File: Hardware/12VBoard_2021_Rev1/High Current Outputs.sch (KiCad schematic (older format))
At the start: 4 parts

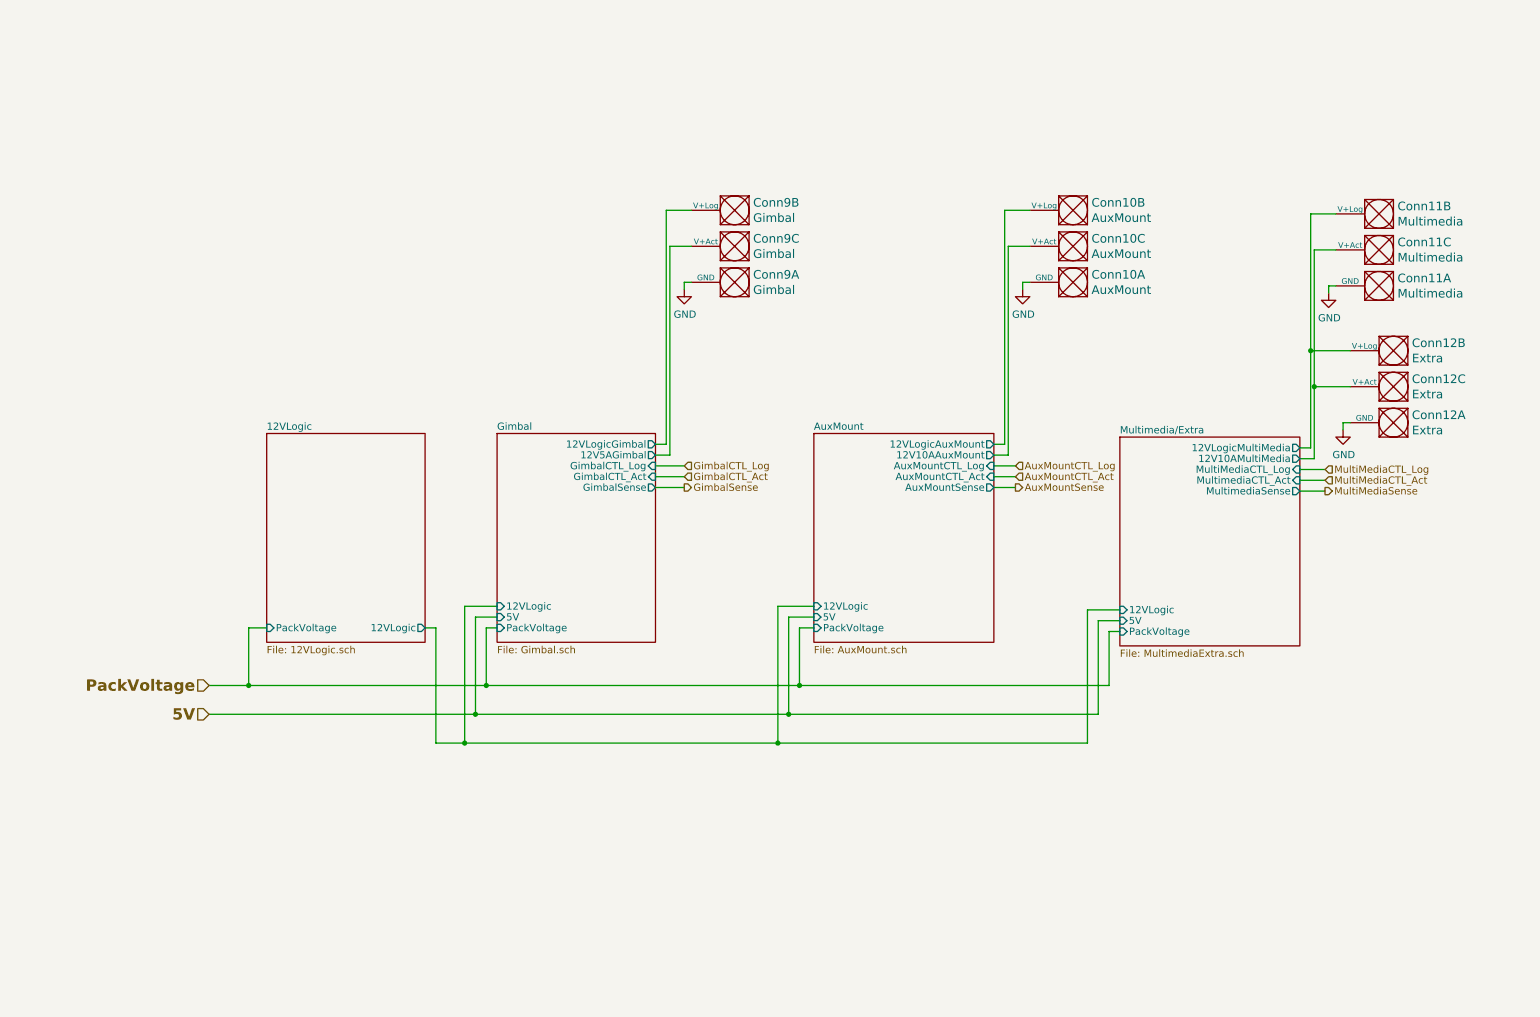
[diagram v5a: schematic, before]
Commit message: changed to big bucks
changed to the bucks used in Master due to a realization in the inductor sizing for the LM5116. It would be much bigger than previous years.
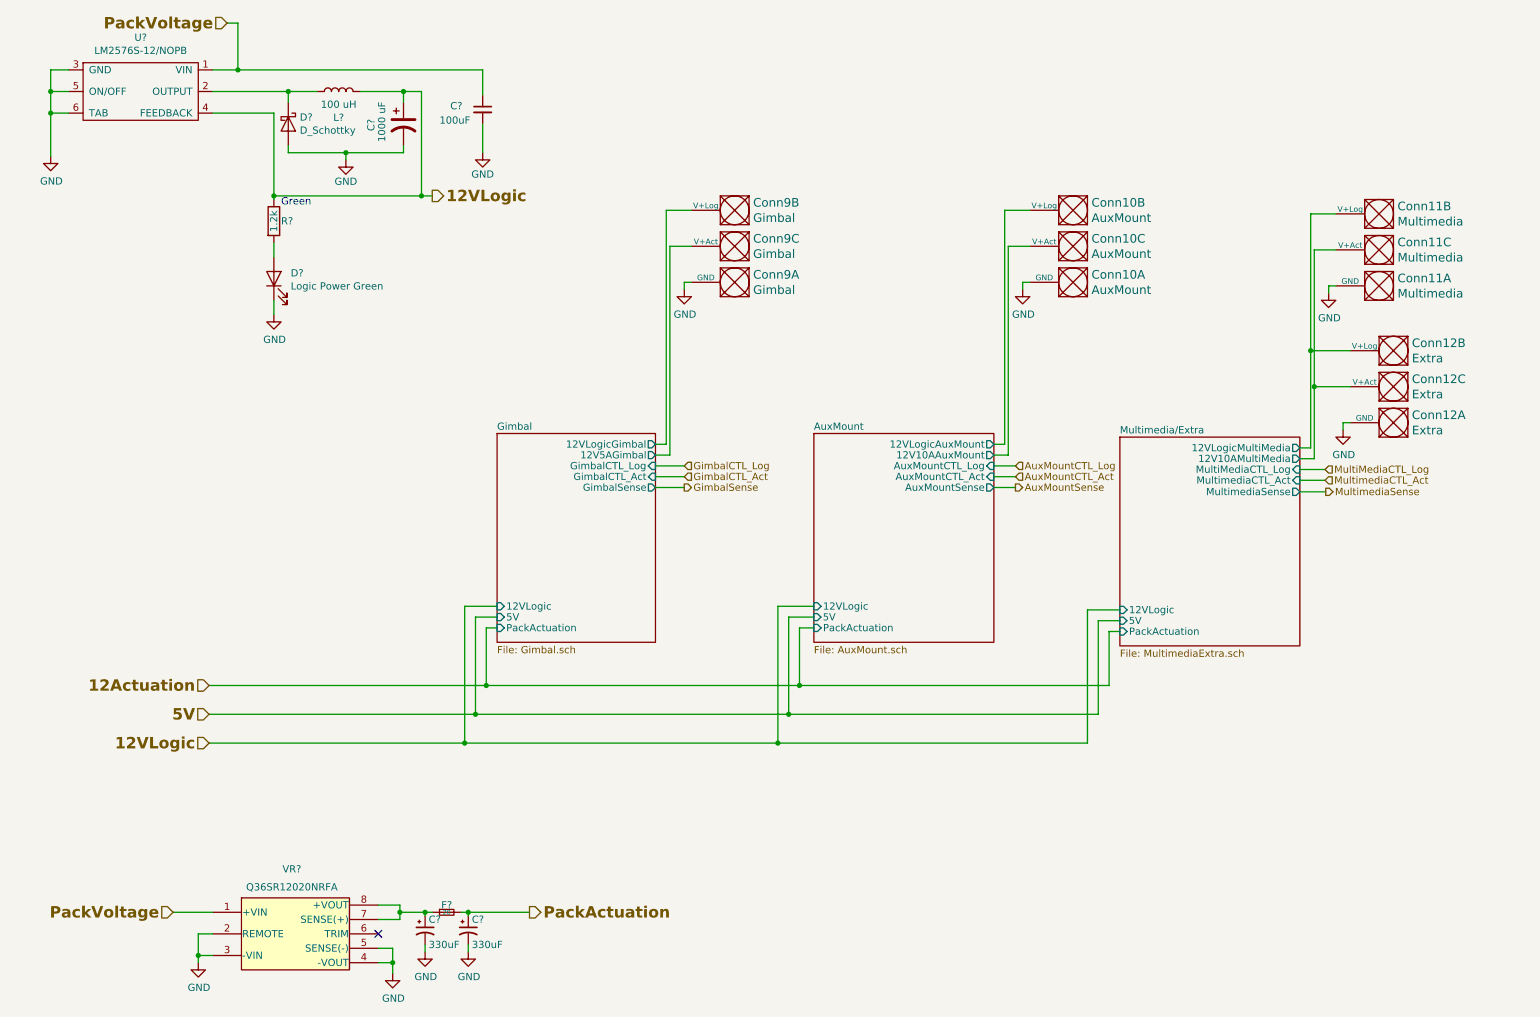
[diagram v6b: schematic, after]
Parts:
- added C? (x2): 330uF, symbol Device:CP1_Small
- added C?: 100uF, Capacitor_SMD:C_0603_1608Metric_Pad1.05x0.95mm_HandSolder, symbol Device:C_Small
- added C?: 1000 uF, Capacitor_THT:CP_Radial_D10.0mm_P5.00mm, symbol Device:CP1
- added D?: D_Schottky, Diode_THT:D_DO-201AD_P5.08mm_Vertical_KathodeUp, symbol Device:D_Schottky
- added D?: Logic Power Green, Diode_SMD:D_0603_1608Metric_Pad1.05x0.95mm_HandSolder, symbol Device:LED
- added F?: 20, symbol Device:Fuse_Small
- added L?: 100 uH, Inductor_SMD:L_0603_1608Metric_Pad1.05x0.95mm_HandSolder, symbol Device:L
- added R?: 1.2k, Resistor_SMD:R_0603_1608Metric_Pad1.05x0.95mm_HandSolder, symbol Device:R
- added U?: LM2576S-12/NOPB, MRDT_Devices:LM2576, symbol 12VBoard_2021_Rev1-rescue:LM2576D2TR4-MRDT_Devices
- added VR?: Q36SR12020NRFA, symbol MRDT_Devices:Q36SR12020NRFA
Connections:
- net GND: now also C?.2, C?.2, C?.2, C?.2, D?.1 (K), D?.2 (A), U?.3 (GND), U?.5 (ON/OFF), U?.6 (TAB), VR?.2 (REMOTE), VR?.3 (-VIN), VR?.4 (-VOUT), VR?.5 (SENSE(-))
- net PackVoltage: now also C?.1, U?.1 (VIN), VR?.1 (+VIN)
- new net: C?.1, F?.1, VR?.7 (SENSE(+)), VR?.8 (+VOUT)
- new net: D?.1 (K), L?.1, U?.2 (OUTPUT)
- new net: D?.2 (A), R?.2
- new net 12VLogic: C?.1, L?.2, R?.1, U?.4 (FEEDBACK)
- new net PackActuation: C?.1, F?.2
- no-connect marks 0 -> 1
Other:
- note added: "Green"

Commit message: Started work on updated layout
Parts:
- C10, C11: renamed from C?; footprint (none) -> Capacitor_THT:CP_Radial_D8.0mm_P3.50mm
- F2: renamed from F?; footprint (none) -> MRDT_Passives:ATC_Fuse_Block
- VR1: renamed from VR?; footprint (none) -> MRDT_Actives:Q36SR12020NRFA
- gave numbers to parts that had none: 7
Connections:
- net PackActuation renamed 12VActuation
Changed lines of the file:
@@
 F5 "5V" I L 6025 4800 49
 F6 "12VLogicAuxMount" O R 7275 3600 50
-F7 "PackActuation" I L 6025 4875 50
+F7 "12VActuation" I L 6025 4875 50
 F8 "12VLogic" I L 6025 4725 50
 F9 "AuxMountCTL_Log" I R 7275 3750 50
@@
 F5 "12VLogicGimbal" O R 4925 3600 50
 F6 "5V" I L 3825 4800 50
-F7 "PackActuation" I L 3825 4875 50
+F7 "12VActuation" I L 3825 4875 50
 F8 "12VLogic" I L 3825 4725 50
 F9 "GimbalCTL_Log" I R 4925 3750 50
@@
 F5 "5V" I L 8150 4825 49
 F6 "12VLogicMultiMedia" O R 9400 3625 50
-F7 "PackActuation" I L 8150 4900 50
+F7 "12VActuation" I L 8150 4900 50
 F8 "12VLogic" I L 8150 4750 50
 F9 "MultiMediaCTL_Log" I R 9400 3775 50
@@
 MultiMediaCTL_Log
 $Comp
-L MRDT_Devices:Q36SR12020NRFA VR?
+L MRDT_Devices:Q36SR12020NRFA VR1
 U 1 1 60547610
 P 2050 7250
-F 0 "VR?" H 2400 7950 50  0000 C CNN
+F 0 "VR1" H 2400 7950 50  0000 C CNN
 F 1 "Q36SR12020NRFA" H 2400 7825 50  0000 C CNN
-F 2 "" H 2350 8050 50  0001 C CNN
+F 2 "MRDT_Actives:Q36SR12020NRFA" H 2350 8050 50  0001 C CNN
 F 3 "" H 2350 8050 50  0001 C CNN
 	1    2050 7250
@@
 	1850 6850 1575 6850
 $Comp
-L power:GND #PWR?
+L power:GND #PWR0101
 U 1 1 6054F874
 P 1750 7200
-F 0 "#PWR?" H 1750 6950 50  0001 C CNN
+F 0 "#PWR0101" H 1750 6950 50  0001 C CNN
 F 1 "GND" H 1755 7027 50  0000 C CNN
 F 2 "" H 1750 7200 50  0001 C CNN
@@
 Connection ~ 3100 7200
 $Comp
-L power:GND #PWR?
+L power:GND #PWR0102
 U 1 1 60562828
 P 3100 7275
-F 0 "#PWR?" H 3100 7025 50  0001 C CNN
+F 0 "#PWR0102" H 3100 7025 50  0001 C CNN
 F 1 "GND" H 3105 7102 50  0000 C CNN
 F 2 "" H 3100 7275 50  0001 C CNN
@@
 	3150 6850 3150 6900
 $Comp
-L Device:CP1_Small C?
+L Device:CP1_Small C10
 U 1 1 6056D755
 P 3325 6975
-F 0 "C?" H 3350 7050 50  0000 L CNN
+F 0 "C10" H 3350 7050 50  0000 L CNN
 F 1 "330uF" H 3350 6875 50  0000 L CNN
-F 2 "" H 3325 6975 50  0001 C CNN
+F 2 "Capacitor_THT:CP_Radial_D8.0mm_P3.50mm" H 3325 6975 50  0001 C CNN
 F 3 "~" H 3325 6975 50  0001 C CNN
 	1    3325 6975
@@
 	3625 6850 4050 6850
 Text HLabel 4050 6850 2    79   Output ~ 16
-PackActuation
-$Comp
-L power:GND #PWR?
+12VActuation
+$Comp
+L power:GND #PWR0103
 U 1 1 60583D08
 P 3325 7125
-F 0 "#PWR?" H 3325 6875 50  0001 C CNN
+F 0 "#PWR0103" H 3325 6875 50  0001 C CNN
 F 1 "GND" H 3330 6952 50  0000 C CNN
 F 2 "" H 3325 7125 50  0001 C CNN
@@
 	3325 7075 3325 7125
 $Comp
-L Device:CP1_Small C?
+L Device:CP1_Small C11
 U 1 1 605915AE
 P 3625 6975
-F 0 "C?" H 3650 7050 50  0000 L CNN
+F 0 "C11" H 3650 7050 50  0000 L CNN
 F 1 "330uF" H 3650 6875 50  0000 L CNN
-F 2 "" H 3625 6975 50  0001 C CNN
+F 2 "Capacitor_THT:CP_Radial_D8.0mm_P3.50mm" H 3625 6975 50  0001 C CNN
 F 3 "~" H 3625 6975 50  0001 C CNN
 	1    3625 6975
@@
 	3625 6875 3625 6850
 $Comp
-L power:GND #PWR?
+L power:GND #PWR0104
 U 1 1 605915B5
 P 3625 7125
-F 0 "#PWR?" H 3625 6875 50  0001 C CNN
+F 0 "#PWR0104" H 3625 6875 50  0001 C CNN
 F 1 "GND" H 3630 6952 50  0000 C CNN
 F 2 "" H 3625 7125 50  0001 C CNN
@@
 	3625 7075 3625 7125
 $Comp
-L Device:Fuse_Small F?
+L Device:Fuse_Small F2
 U 1 1 60594467
 P 3475 6850
-F 0 "F?" H 3475 6900 50  0000 C CNN
+F 0 "F2" H 3475 6900 50  0000 C CNN
 F 1 "20" H 3475 6850 31  0000 C CNN
-F 2 "" H 3475 6850 50  0001 C CNN
+F 2 "MRDT_Passives:ATC_Fuse_Block" H 3475 6850 50  0001 C CNN
 F 3 "~" H 3475 6850 50  0001 C CNN
 	1    3475 6850
@@
 AR Path="/5F74F36B/5F971CD6/605D6402" Ref="#PWR?"  Part="1"
 AR Path="/5F74F36B/5F8236F9/605D6402" Ref="#PWR?"  Part="1"
-AR Path="/5F74F36B/605D6402" Ref="#PWR?"  Part="1"
+AR Path="/5F74F36B/605D6402" Ref="#PWR0105"  Part="1"
 AR Path="/5F74F36B/5FB68F3E/605D6402" Ref="#PWR?"  Part="1"
-F 0 "#PWR?" H 2275 2450 50  0001 C CNN
+F 0 "#PWR0105" H 2275 2450 50  0001 C CNN
 F 1 "GND" H 2280 2527 50  0000 C CNN
 F 2 "" H 2275 2700 50  0001 C CNN
@@
 AR Path="/5F74F36B/5F971CD6/605D6408" Ref="D?"  Part="1"
 AR Path="/5F74F36B/5F8236F9/605D6408" Ref="D?"  Part="1"
-AR Path="/5F74F36B/605D6408" Ref="D?"  Part="1"
+AR Path="/5F74F36B/605D6408" Ref="D1"  Part="1"
 AR Path="/5F74F36B/5FB68F3E/605D6408" Ref="D?"  Part="1"
-F 0 "D?" V 2314 2333 50  0000 R CNN
+F 0 "D1" V 2314 2333 50  0000 R CNN
 F 1 "Logic Power Green" V 2223 2333 50  0000 R CNN
 F 2 "Diode_SMD:D_0603_1608Metric_Pad1.05x0.95mm_HandSolder" H 2275 2450 50  0001 C CNN
@@
 AR Path="/5F74F36B/5F971CD6/605D63FC" Ref="R?"  Part="1"
 AR Path="/5F74F36B/5F8236F9/605D63FC" Ref="R?"  Part="1"
-AR Path="/5F74F36B/605D63FC" Ref="R?"  Part="1"
+AR Path="/5F74F36B/605D63FC" Ref="R8"  Part="1"
 AR Path="/5F74F36B/5FB68F3E/605D63FC" Ref="R?"  Part="1"
-F 0 "R?" H 2325 2050 50  0000 L CNN
+F 0 "R8" H 2325 2050 50  0000 L CNN
 F 1 "1.2k" V 2275 1975 50  0000 L CNN
 F 2 "Resistor_SMD:R_0603_1608Metric_Pad1.05x0.95mm_HandSolder" V 2205 2050 50  0001 C CNN
@@
 AR Path="/5F74F223/605D63F4" Ref="#PWR?"  Part="1"
 AR Path="/5F74F36B/5F8236F9/605D63F4" Ref="#PWR?"  Part="1"
-AR Path="/5F74F36B/605D63F4" Ref="#PWR?"  Part="1"
+AR Path="/5F74F36B/605D63F4" Ref="#PWR0106"  Part="1"
 AR Path="/5F74F36B/5FB68F3E/605D63F4" Ref="#PWR?"  Part="1"
-F 0 "#PWR?" H 3725 1325 50  0001 C CNN
+F 0 "#PWR0106" H 3725 1325 50  0001 C CNN
 F 1 "GND" H 3725 1425 50  0000 C CNN
 F 2 "" H 3725 1575 50  0001 C CNN
@@
 AR Path="/5F74F223/605D63EE" Ref="L?"  Part="1"
 AR Path="/5F74F36B/5F8236F9/605D63EE" Ref="L?"  Part="1"
-AR Path="/5F74F36B/605D63EE" Ref="L?"  Part="1"
+AR Path="/5F74F36B/605D63EE" Ref="L1"  Part="1"
 AR Path="/5F74F36B/5FB68F3E/605D63EE" Ref="L?"  Part="1"
-F 0 "L?" V 2544 1150 50  0000 C CNN
+F 0 "L1" V 2544 1150 50  0000 C CNN
 F 1 "100 uH" V 2635 1150 50  0000 C CNN
 F 2 "Inductor_SMD:L_0603_1608Metric_Pad1.05x0.95mm_HandSolder" H 2725 1150 50  0001 C CNN
@@
 AR Path="/5F74F223/605D63E8" Ref="C?"  Part="1"
 AR Path="/5F74F36B/5F8236F9/605D63E8" Ref="C?"  Part="1"
-AR Path="/5F74F36B/605D63E8" Ref="C?"  Part="1"
+AR Path="/5F74F36B/605D63E8" Ref="C9"  Part="1"
 AR Path="/5F74F36B/5FB68F3E/605D63E8" Ref="C?"  Part="1"
-F 0 "C?" V 2950 1325 50  0000 L CNN
+F 0 "C9" V 2950 1325 50  0000 L CNN
 F 1 "1000 uF" V 3025 1250 50  0000 L CNN
 F 2 "Capacitor_THT:CP_Radial_D10.0mm_P5.00mm" H 3175 1375 50  0001 C CNN
@@
 AR Path="/5F74F223/605D63E2" Ref="#PWR?"  Part="1"
 AR Path="/5F74F36B/5F8236F9/605D63E2" Ref="#PWR?"  Part="1"
-AR Path="/5F74F36B/605D63E2" Ref="#PWR?"  Part="1"
+AR Path="/5F74F36B/605D63E2" Ref="#PWR0107"  Part="1"
 AR Path="/5F74F36B/5FB68F3E/605D63E2" Ref="#PWR?"  Part="1"
-F 0 "#PWR?" H 2775 1375 50  0001 C CNN
+F 0 "#PWR0107" H 2775 1375 50  0001 C CNN
 F 1 "GND" H 2775 1475 50  0000 C CNN
 F 2 "" H 2775 1625 50  0001 C CNN
@@
 AR Path="/5F74F223/605D63DC" Ref="U?"  Part="1"
 AR Path="/5F74F36B/5F8236F9/605D63DC" Ref="U?"  Part="1"
-AR Path="/5F74F36B/605D63DC" Ref="U?"  Part="1"
+AR Path="/5F74F36B/605D63DC" Ref="U6"  Part="1"
 AR Path="/5F74F36B/5FB68F3E/605D63DC" Ref="U?"  Part="1"
-F 0 "U?" H 1350 1625 50  0000 C CNN
+F 0 "U6" H 1350 1625 50  0000 C CNN
 F 1 "LM2576S-12/NOPB" H 1350 1534 50  0000 C CNN
 F 2 "MRDT_Devices:LM2576" H 1350 1650 50  0001 C CNN
@@
 AR Path="/5F74F223/605D63D6" Ref="#PWR?"  Part="1"
 AR Path="/5F74F36B/5F8236F9/605D63D6" Ref="#PWR?"  Part="1"
-AR Path="/5F74F36B/605D63D6" Ref="#PWR?"  Part="1"
+AR Path="/5F74F36B/605D63D6" Ref="#PWR0108"  Part="1"
 AR Path="/5F74F36B/5FB68F3E/605D63D6" Ref="#PWR?"  Part="1"
-F 0 "#PWR?" H 725 1350 50  0001 C CNN
+F 0 "#PWR0108" H 725 1350 50  0001 C CNN
 F 1 "GND" H 730 1427 50  0000 C CNN
 F 2 "" H 725 1600 50  0001 C CNN
@@
 AR Path="/5F74F223/605D63B9" Ref="D?"  Part="1"
 AR Path="/5F74F36B/5F8236F9/605D63B9" Ref="D?"  Part="1"
-AR Path="/5F74F36B/605D63B9" Ref="D?"  Part="1"
+AR Path="/5F74F36B/605D63B9" Ref="D3"  Part="1"
 AR Path="/5F74F36B/5FB68F3E/605D63B9" Ref="D?"  Part="1"
-F 0 "D?" V 2329 1455 50  0000 L CNN
+F 0 "D3" V 2329 1455 50  0000 L CNN
 F 1 "D_Schottky" V 2420 1455 50  0000 L CNN
 F 2 "Diode_THT:D_DO-201AD_P5.08mm_Vertical_KathodeUp" H 2375 1375 50  0001 C CNN
@@
 AR Path="/5F74F223/605D63B3" Ref="C?"  Part="1"
 AR Path="/5F74F36B/5F8236F9/605D63B3" Ref="C?"  Part="1"
-AR Path="/5F74F36B/605D63B3" Ref="C?"  Part="1"
+AR Path="/5F74F36B/605D63B3" Ref="C12"  Part="1"
 AR Path="/5F74F36B/5FB68F3E/605D63B3" Ref="C?"  Part="1"
-F 0 "C?" H 3500 1300 50  0000 L CNN
+F 0 "C12" H 3500 1300 50  0000 L CNN
 F 1 "100uF" H 3425 1200 50  0000 L CNN
 F 2 "Capacitor_SMD:C_0603_1608Metric_Pad1.05x0.95mm_HandSolder" H 3725 1275 50  0001 C CNN

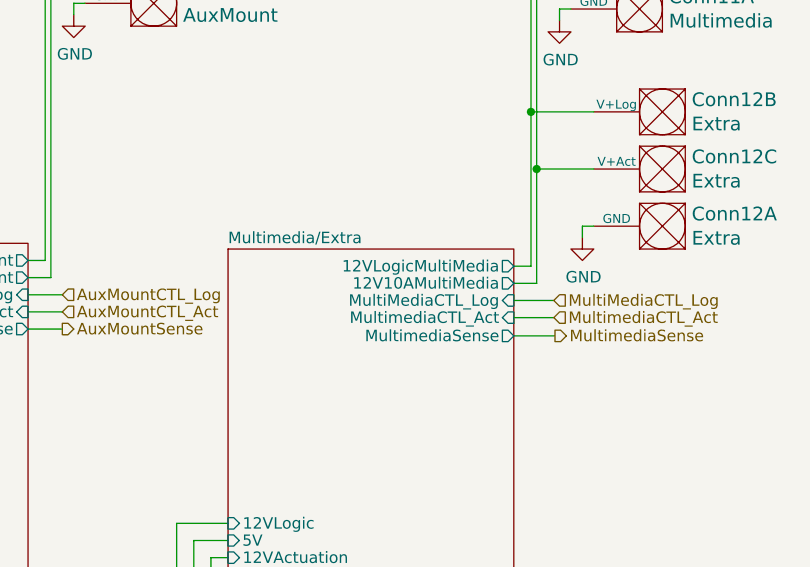
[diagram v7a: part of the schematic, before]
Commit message: Layout for high current
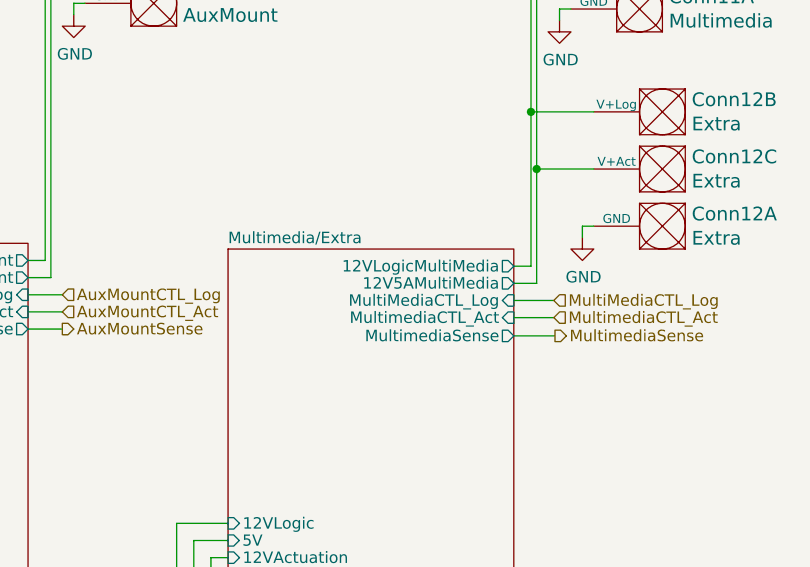
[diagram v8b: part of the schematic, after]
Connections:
- net Multimedia/Extra/12V10AMultiMedia renamed Multimedia/Extra/12V5AMultiMedia
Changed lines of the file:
@@
 F0 "Multimedia/Extra" 50
 F1 "MultimediaExtra.sch" 50
-F2 "12V10AMultiMedia" O R 9400 3700 50
+F2 "12V5AMultiMedia" O R 9400 3700 50
 F3 "MultimediaCTL_Act" I R 9400 3850 50
 F4 "MultimediaSense" O R 9400 3930 50
